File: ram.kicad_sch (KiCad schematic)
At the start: 43 parts, among them IC5 MT41K256M16TW-107_P

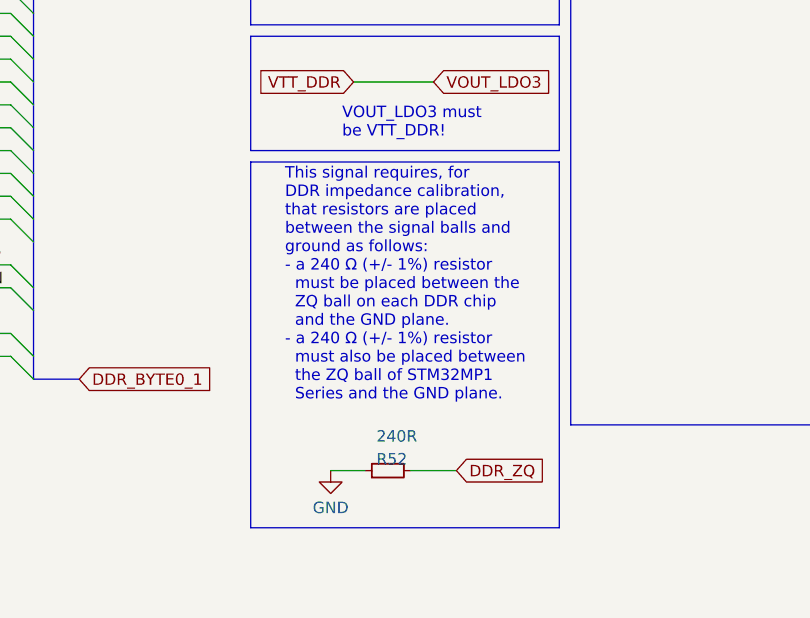
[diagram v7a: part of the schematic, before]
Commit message: Add Uart to MPU
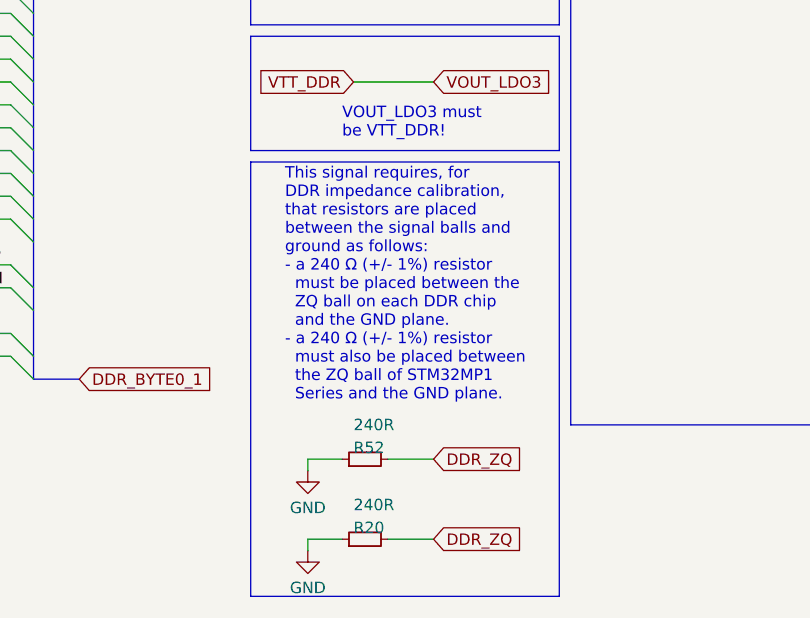
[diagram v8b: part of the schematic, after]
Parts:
- added R20: 240R, symbol Device:R_Small
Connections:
- net DDR_ZQ: now also R20.2
- net GND: now also R20.1
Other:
- moved on the sheet: R52
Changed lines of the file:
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@@
+    (stroke (width 0) (type default))
+  )
+  (wire (pts (xy 142.24 147.32) (xy 142.24 148.59))
     (stroke (width 0) (type default))
   )
@@
     (stroke (width 0) (type default))
   )
+  (wire (pts (xy 142.24 138.43) (xy 142.24 139.7))
+    (stroke (width 0) (type default))
+  )
   (wire (pts (xy 142.24 30.48) (xy 140.97 30.48))
     (stroke (width 0) (type default))
@@
     (stroke (width 0) (type default))
   )
+  (wire (pts (xy 151.13 147.32) (xy 156.21 147.32))
+    (stroke (width 0) (type default))
+  )
   (wire (pts (xy 264.16 119.38) (xy 274.32 119.38))
     (stroke (width 0) (type default))
@@
     (stroke (width 0) (type default))
   )
-  (wire (pts (xy 148.59 139.7) (xy 144.78 139.7))
+  (wire (pts (xy 146.05 138.43) (xy 142.24 138.43))
     (stroke (width 0) (type default))
   )
@@
     (stroke (width 0) (type default))
   )
+  (wire (pts (xy 146.05 147.32) (xy 142.24 147.32))
+    (stroke (width 0) (type default))
+  )
   (bus (pts (xy 45.72 73.66) (xy 45.72 76.2))
     (stroke (width 0) (type default))
@@
     (stroke (width 0) (type default))
   )
-  (wire (pts (xy 153.67 139.7) (xy 158.75 139.7))
+  (wire (pts (xy 151.13 138.43) (xy 156.21 138.43))
     (stroke (width 0) (type default))
   )
@@
     (fill (type none))
   )
-  (rectangle (start 135.89 105.41) (end 170.18 146.05)
+  (rectangle (start 135.89 105.41) (end 170.18 153.67)
     (stroke (width 0) (type default))
     (fill (type none))
@@
     (effects (font (size 1.27 1.27)) (justify left bottom))
   )
-  (global_label "DDR_ZQ" (shape input) (at 158.75 139.7 0) (fields_autoplaced)
+  (global_label "DDR_ZQ" (shape input) (at 156.21 138.43 0) (fields_autoplaced)
     (effects (font (size 1.27 1.27)) (justify left))
   )
@@
     )
   )
+  (global_label "DDR_ZQ" (shape input) (at 156.21 147.32 0) (fields_autoplaced)
+    (effects (font (size 1.27 1.27)) (justify left))
+    (property "Intersheetrefs" "${INTERSHEET_REFS}" (at -2.54 7.62 0)
+      (effects (font (size 1.27 1.27)) hide)
+    )
+  )
   (global_label "DDR_RESETN" (shape input) (at 149.86 41.91 0) (fields_autoplaced)
     (effects (font (size 1.27 1.27)) (justify left))
@@
         (path "/017c50c6-333c-4d31-ad5a-278994a09b14/f5831ad7-86f4-4338-9d6c-a9943f11383a"
           (reference "R42") (unit 1)
+        )
+      )
+    )
+  )
+  (symbol (lib_id "Device:R_Small") (at 148.59 147.32 90) (unit 1)
+    (in_bom yes) (on_board yes) (dnp no)
+    (property "Reference" "R20" (at 147.32 146.05 90)
+      (effects (font (size 1.27 1.27)) (justify right))
+    )
+    (property "Value" "240R" (at 147.32 143.51 90)
+      (effects (font (size 1.27 1.27)) (justify right))
+    )
+    (property "Footprint" "" (at 148.59 147.32 0)
+      (effects (font (size 1.27 1.27)) hide)
+    )
+    (property "Datasheet" "~" (at 148.59 147.32 0)
+      (effects (font (size 1.27 1.27)) hide)
+    )
+    (pin "1")
+    (pin "2")
+    (instances
+      (project "gba"
+        (path "/017c50c6-333c-4d31-ad5a-278994a09b14/f5831ad7-86f4-4338-9d6c-a9943f11383a"
+          (reference "R20") (unit 1)
         )
       )
@@
     )
   )
+  (symbol (lib_id "power:GND") (at 142.24 148.59 0) (unit 1)
+    (in_bom yes) (on_board yes) (dnp no) (fields_autoplaced)
+    (property "Reference" "#PWR052" (at 142.24 154.94 0)
+      (effects (font (size 1.27 1.27)) hide)
+    )
+    (property "Value" "GND" (at 142.24 152.7255 0)
+      (effects (font (size 1.27 1.27)))
+    )
+    (property "Footprint" "" (at 142.24 148.59 0)
+      (effects (font (size 1.27 1.27)) hide)
+    )
+    (property "Datasheet" "" (at 142.24 148.59 0)
+      (effects (font (size 1.27 1.27)) hide)
+    )
+    (pin "1")
+    (instances
+      (project "gba"
+        (path "/017c50c6-333c-4d31-ad5a-278994a09b14/f5831ad7-86f4-4338-9d6c-a9943f11383a"
+          (reference "#PWR052") (unit 1)
+        )
+      )
+    )
+  )
   (symbol (lib_id "Device:R_Small") (at 232.41 30.48 90) (unit 1)
     (in_bom yes) (on_board yes) (dnp no) (fields_autoplaced)
@@
     )
   )
-  (symbol (lib_id "Device:R_Small") (at 151.13 139.7 90) (unit 1)
+  (symbol (lib_id "Device:R_Small") (at 148.59 138.43 90) (unit 1)
     (in_bom yes) (on_board yes) (dnp no)
-    (property "Reference" "R52" (at 149.86 138.43 90)
+    (property "Reference" "R52" (at 147.32 137.16 90)
       (effects (font (size 1.27 1.27)) (justify right))
     )
-    (property "Value" "240R" (at 149.86 135.89 90)
+    (property "Value" "240R" (at 147.32 134.62 90)
       (effects (font (size 1.27 1.27)) (justify right))
     )
-    (property "Footprint" "" (at 151.13 139.7 0)
-      (effects (font (size 1.27 1.27)) hide)
-    )
-    (property "Datasheet" "~" (at 151.13 139.7 0)
+    (property "Footprint" "" (at 148.59 138.43 0)
+      (effects (font (size 1.27 1.27)) hide)
+    )
+    (property "Datasheet" "~" (at 148.59 138.43 0)
       (effects (font (size 1.27 1.27)) hide)
     )
@@
     )
   )
-  (symbol (lib_id "power:GND") (at 144.78 139.7 0) (unit 1)
-    (in_bom yes) (on_board yes) (dnp no) (fields_autoplaced)
-    (property "Reference" "#PWR063" (at 144.78 146.05 0)
-      (effects (font (size 1.27 1.27)) hide)
-    )
-    (property "Value" "GND" (at 144.78 143.8355 0)
-      (effects (font (size 1.27 1.27)))
-    )
-    (property "Footprint" "" (at 144.78 139.7 0)
-      (effects (font (size 1.27 1.27)) hide)
-    )
-    (property "Datasheet" "" (at 144.78 139.7 0)
-      (effects (font (size 1.27 1.27)) hide)
-    )
+  (symbol (lib_id "power:GND") (at 142.24 139.7 0) (unit 1)
+    (in_bom yes) (on_board yes) (dnp no) (fields_autoplaced)
+    (property "Reference" "#PWR063" (at 142.24 146.05 0)
+      (effects (font (size 1.27 1.27)) hide)
+    )
+    (property "Value" "GND" (at 142.24 143.8355 0)
+      (effects (font (size 1.27 1.27)))
+    )
+    (property "Footprint" "" (at 142.24 139.7 0)
+      (effects (font (size 1.27 1.27)) hide)
+    )
+    (property "Datasheet" "" (at 142.24 139.7 0)
+      (effects (font (size 1.27 1.27)) hide)
+    )
